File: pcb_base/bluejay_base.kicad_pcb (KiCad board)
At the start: 2 copper layers, 147 x 140.5 mm, 10 parts

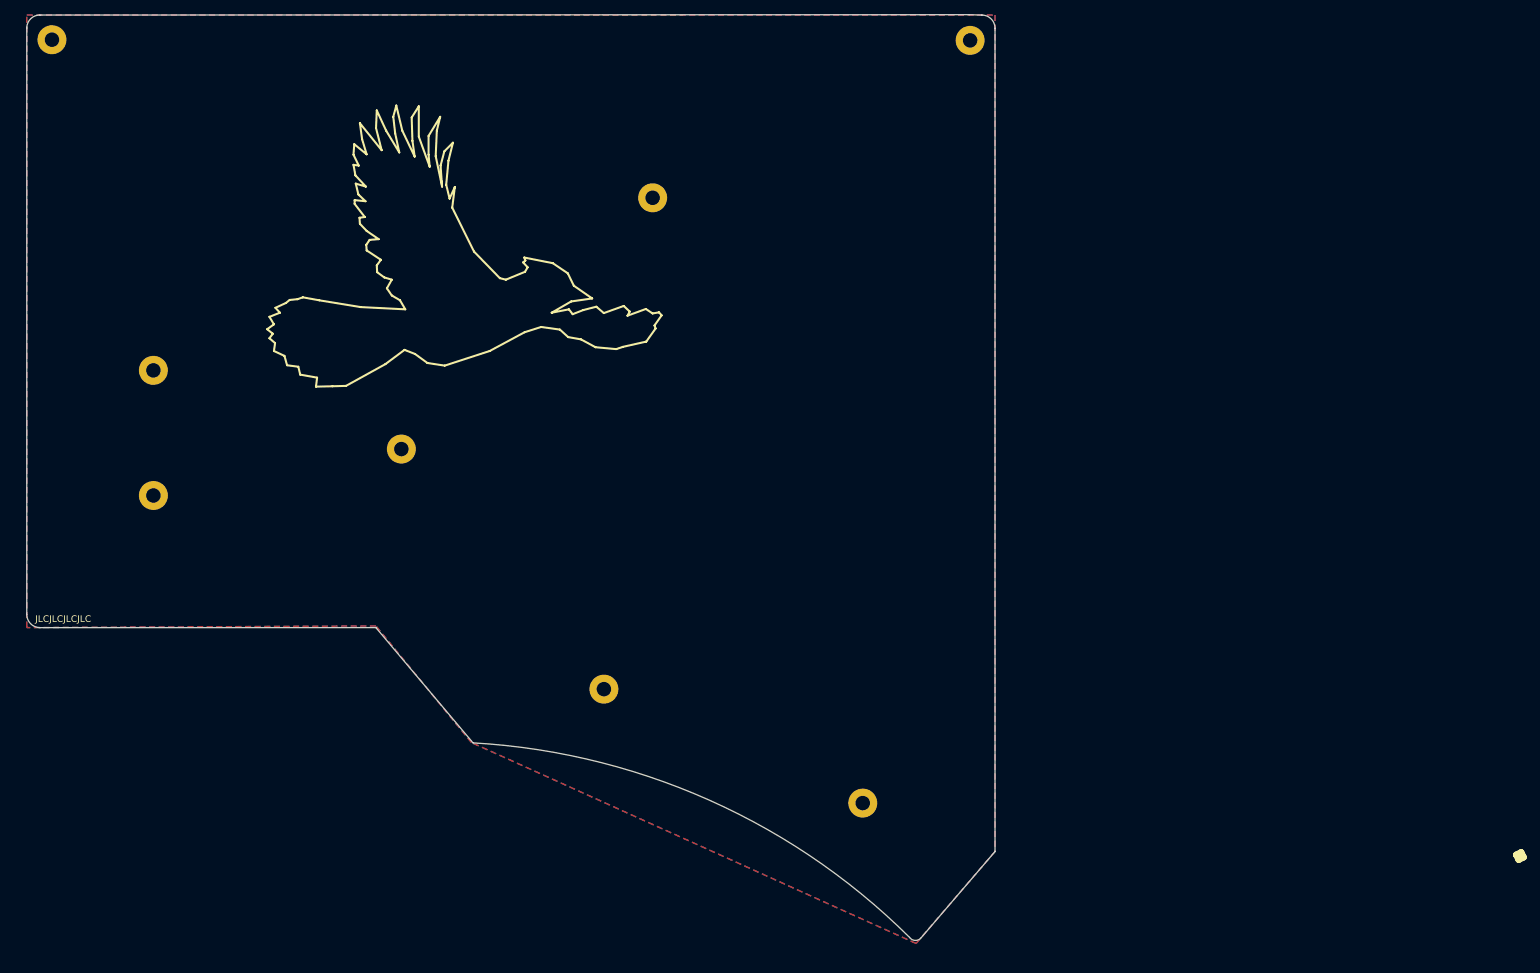
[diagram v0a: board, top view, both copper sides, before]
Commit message: Round edges of PCB
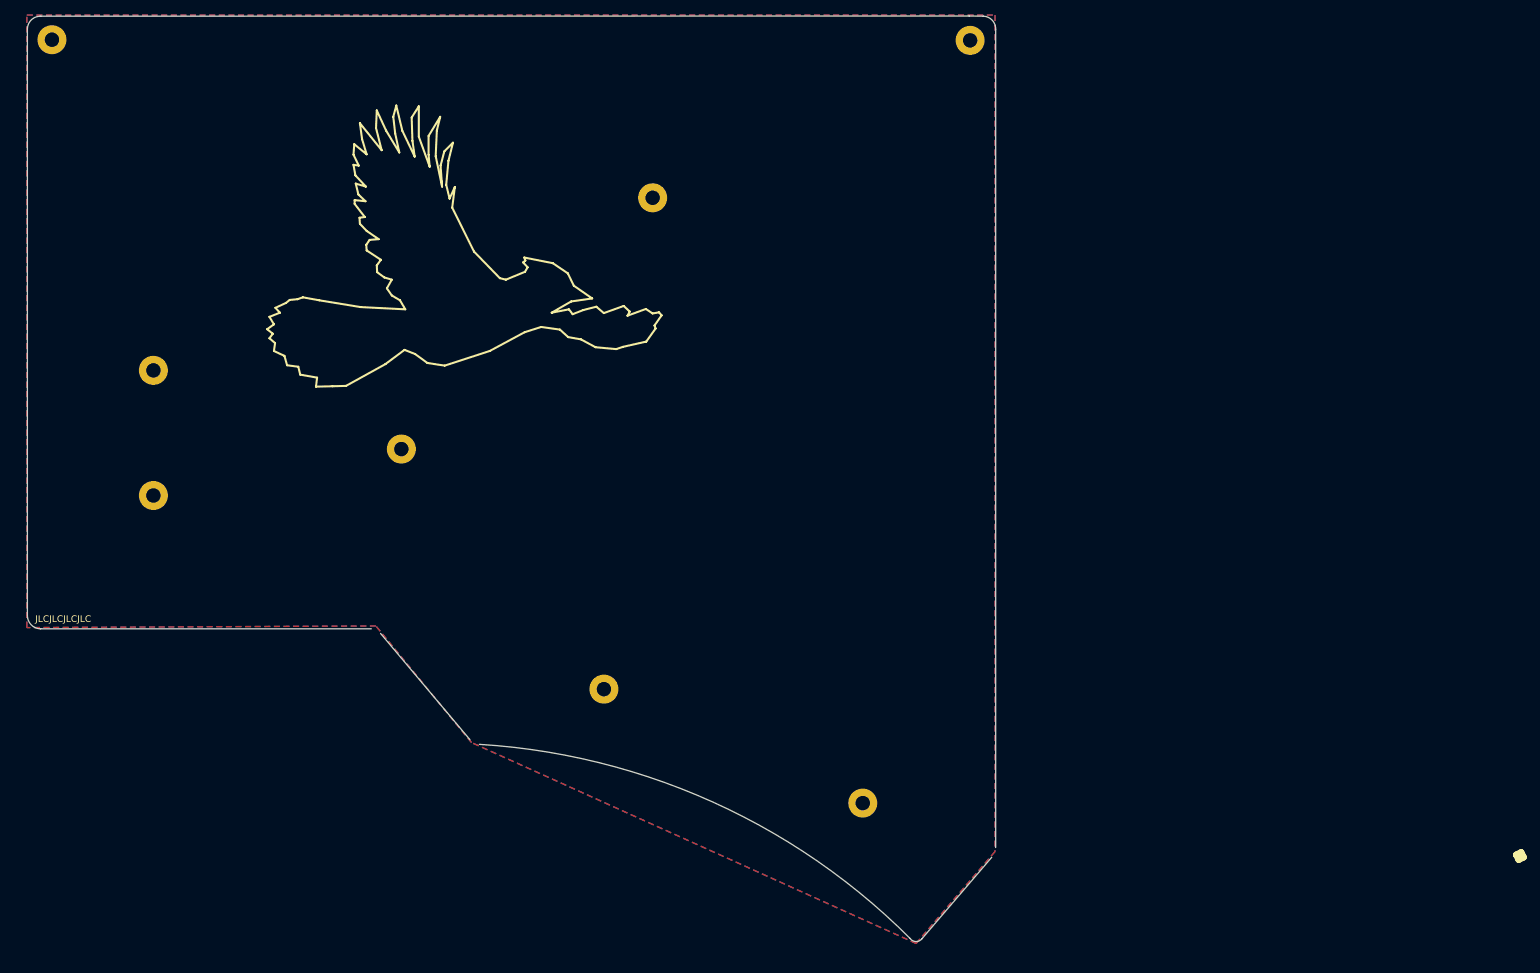
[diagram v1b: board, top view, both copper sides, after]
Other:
- outline, holes or cut-outs redrawn
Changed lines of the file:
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@@
   (gr_line locked (start 26.028999 -42.674998) (end 26.028999 -42.674998) (layer "Eco1.User") (width 0.188976))
   (gr_line locked (start -16.546013 52.286989) (end -16.546013 38.286989) (layer "Eco1.User") (width 0.188976))
-  (gr_line (start 60.9812 70.6563) (end 49.7812 83.7263) (layer "Edge.Cuts") (width 0.1))
-  (gr_arc (start -18.2688 54.1563) (mid 17.583107 62.841492) (end 48.0112 83.6963) (layer "Edge.Cuts") (width 0.1))
-  (gr_arc (start 58.9812 -56.3437) (mid 60.393459 -55.755959) (end 60.981199 -54.3437) (layer "Edge.Cuts") (width 0.1))
-  (gr_line (start 60.9812 70.6563) (end 60.981199 -54.3437) (layer "Edge.Cuts") (width 0.1))
-  (gr_arc (start -86.024489 -54.35145) (mid -85.442713 -55.767431) (end -84.024489 -56.3437) (layer "Edge.Cuts") (width 0.1))
-  (gr_arc (start -84.02552 36.663017) (mid -85.443204 36.061839) (end -86.025519 34.6363) (layer "Edge.Cuts") (width 0.1))
-  (gr_line (start -86.024489 -54.35145) (end -86.025519 34.6363) (layer "Edge.Cuts") (width 0.1))
-  (gr_line (start -84.02552 36.663017) (end -33.0188 36.6563) (layer "Edge.Cuts") (width 0.1))
-  (gr_line (start -33.0188 36.6563) (end -18.2688 54.1563) (layer "Edge.Cuts") (width 0.1))
-  (gr_line (start 58.9812 -56.3437) (end 57.05 -56.4) (layer "Edge.Cuts") (width 0.1))
-  (gr_line (start 57.05 -56.4) (end -84.024489 -56.3437) (layer "Edge.Cuts") (width 0.1))
-  (gr_arc (start 49.7812 83.7263) (mid 48.888799 84.147698) (end 48.0112 83.6963) (layer "Edge.Cuts") (width 0.1))
+  (gr_line (start 60.48 71.53) (end 49.88 83.9) (layer "Edge.Cuts") (width 0.1))
+  (gr_arc (start -17.32 54.38) (mid 18.101214 63.120674) (end 48.11 83.87) (layer "Edge.Cuts") (width 0.1))
+  (gr_arc (start 59.2 -56.175) (mid 60.553201 -55.55994) (end 61.08 -54.17) (layer "Edge.Cuts") (width 0.1))
+  (gr_line (start 61.08 70.05) (end 61.08 -54.17) (layer "Edge.Cuts") (width 0.1))
+  (gr_arc (start -85.93 -54.18) (mid -85.347749 -55.594848) (end -83.93 -56.17) (layer "Edge.Cuts") (width 0.1))
+  (gr_arc (start -83.93 36.84) (mid -85.348353 36.23717) (end -85.93 34.81) (layer "Edge.Cuts") (width 0.1))
+  (gr_line (start -85.93 34.81) (end -85.93 -54.18) (layer "Edge.Cuts") (width 0.1))
+  (gr_line (start -83.93 36.84) (end -33.72 36.84) (layer "Edge.Cuts") (width 0.1))
+  (gr_line (start -32.31 37.54) (end -18.73 53.68) (layer "Edge.Cuts") (width 0.1))
+  (gr_line (start 59.2 -56.175) (end 57.05 -56.2) (layer "Edge.Cuts") (width 0.1))
+  (gr_line (start 57.05 -56.2) (end -83.93 -56.17) (layer "Edge.Cuts") (width 0.1))
+  (gr_arc (start 49.88 83.9) (mid 48.987603 84.321434) (end 48.11 83.87) (layer "Edge.Cuts") (width 0.1))
+  (gr_arc (start -33.72 36.84) (mid -32.960504 37.08023) (end -32.31 37.54) (layer "F.Fab") (width 0.1))
+  (gr_arc (start 61.08 70.05) (mid 60.863331 70.823783) (end 60.48 71.53) (layer "F.Fab") (width 0.1))
+  (gr_arc (start -17.32 54.38) (mid -18.079496 54.13977) (end -18.73 53.68) (layer "F.Fab") (width 0.1))
   (gr_text "JLCJLCJLCJLC" (at -80.5 35.33) (layer "F.SilkS")
     (effects (font (size 1 1) (thickness 0.15)))

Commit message: Update placement of some components and size of drill holes
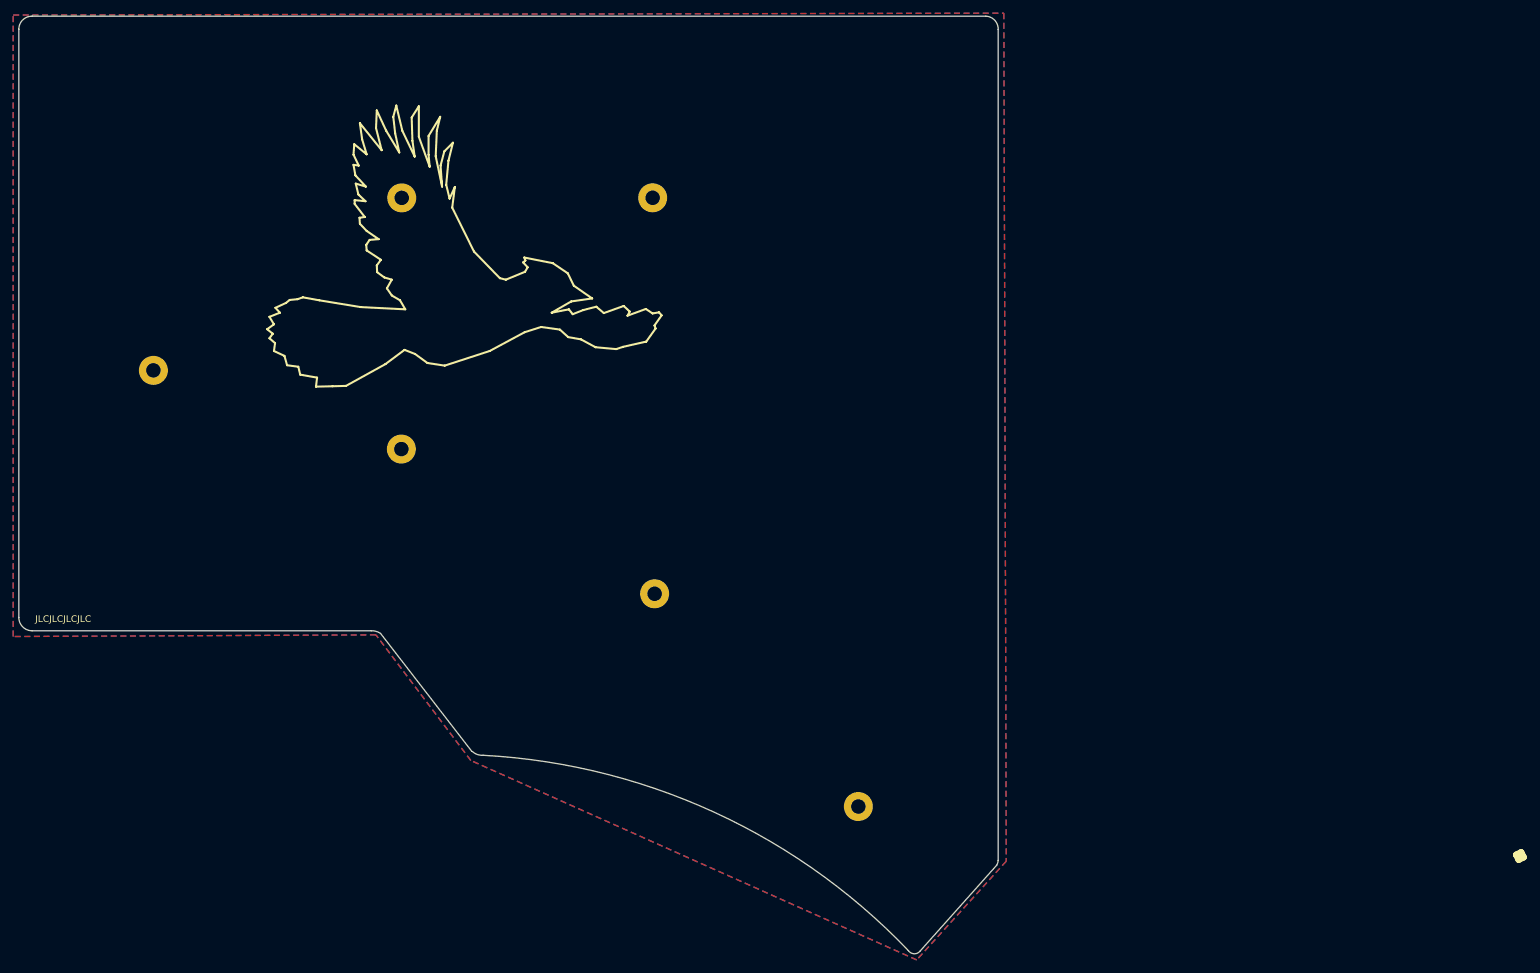
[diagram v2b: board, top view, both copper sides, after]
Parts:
- removed H7, H8: M2, MountingHole:MountingHole_2.2mm_M2_Pad
- moved H2 97.6 mm to (40.2, 63.8)
- moved H6 77.5 mm to (9.30, 31.5)
- moved H1 58.3 mm to (-29.1, -28.6)
- moved H3 53.8 mm to (9.00, -28.6)
- renumbered H3 to H2, H2 to H3
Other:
- board size 147 x 140.5 mm -> 148.7 x 142.3 mm
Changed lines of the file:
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@@
   (net 1 "GND")
-  (footprint "MountingHole:MountingHole_2.2mm_M2_Pad" (layer "F.Cu")
-    (at 40.9 63.3)
-    (descr "Mounting Hole 2.2mm, M2")
-    (tags "mounting hole 2.2mm m2")
-    (property "Sheetfile" "bluejay_base.kicad_sch")
-    (property "Sheetname" "")
-    (property "exclude_from_bom" "")
-    (attr exclude_from_pos_files exclude_from_bom)
-    (fp_text reference "H8" (at 0 -3.2) (layer "F.Fab")
-      (effects (font (size 1 1) (thickness 0.15)))
-    )
-    (fp_text value "M2" (at 0 3.2) (layer "F.Fab")
-      (effects (font (size 1 1) (thickness 0.15)))
-    )
-    (fp_text user "${REFERENCE}" (at 0 0) (layer "F.Fab")
-      (effects (font (size 1 1) (thickness 0.15)))
-    )
-    (fp_circle (center 0 0) (end 2.2 0) (layer "Cmts.User") (width 0.15) (fill none))
-    (fp_circle (center 0 0) (end 2.45 0) (layer "F.CrtYd") (width 0.05) (fill none))
-    (pad "1" thru_hole circle (at 0 0) (size 4.4 4.4) (drill 2.2) (layers *.Cu *.Mask))
-  )
   (footprint "MountingHole:MountingHole_2.2mm_M2_Pad" (layer "F.Cu")
     (at -29.15 9.55)
@@
   )
   (footprint "MountingHole:MountingHole_2.2mm_M2_Pad" (layer "F.Cu")
-    (at -82.2 -52.6)
+    (at -29.09 -28.59)
     (descr "Mounting Hole 2.2mm, M2")
     (tags "mounting hole 2.2mm m2")
@@
     (fp_circle (center 0 0) (end 2.45 0) (layer "F.CrtYd") (width 0.05) (fill none))
     (pad "1" thru_hole circle (at 0 0) (size 4.4 4.4) (drill 2.2) (layers *.Cu *.Mask))
-  )
-  (footprint "MountingHole:MountingHole_2.2mm_M2_Pad" (layer "F.Cu")
-    (at 1.6 46)
-    (descr "Mounting Hole 2.2mm, M2")
-    (tags "mounting hole 2.2mm m2")
-    (property "Sheetfile" "bluejay_base.kicad_sch")
-    (property "Sheetname" "")
-    (property "exclude_from_bom" "")
-    (attr exclude_from_pos_files exclude_from_bom)
-    (fp_text reference "H7" (at 0 -3.2) (layer "F.Fab")
-      (effects (font (size 1 1) (thickness 0.15)))
-    )
-    (fp_text value "M2" (at 0 3.2) (layer "F.Fab")
-      (effects (font (size 1 1) (thickness 0.15)))
-    )
-    (fp_text user "${REFERENCE}" (at 0 0) (layer "F.Fab")
-      (effects (font (size 1 1) (thickness 0.15)))
-    )
-    (fp_circle (center 0 0) (end 2.2 0) (layer "Cmts.User") (width 0.15) (fill none))
-    (fp_circle (center 0 0) (end 2.45 0) (layer "F.CrtYd") (width 0.05) (fill none))
-    (pad "1" thru_hole circle (at 0 0) (size 4.4 4.4) (drill 2.2) (layers *.Cu *.Mask))
-  )
-  (footprint "MountingHole:MountingHole_2.2mm_M2_Pad" (layer "F.Cu")
-    (at 57.2 -52.5)
-    (descr "Mounting Hole 2.2mm, M2")
-    (tags "mounting hole 2.2mm m2")
-    (property "Sheetfile" "bluejay_base.kicad_sch")
-    (property "Sheetname" "")
-    (attr exclude_from_pos_files)
-    (fp_text reference "H2" (at 0 -3.2) (layer "F.Fab")
-      (effects (font (size 1 1) (thickness 0.15)))
-    )
-    (fp_text value "M2" (at 0 3.2) (layer "F.Fab")
-      (effects (font (size 1 1) (thickness 0.15)))
-    )
-    (fp_text user "${REFERENCE}" (at 0 0) (layer "F.Fab")
-      (effects (font (size 1 1) (thickness 0.15)))
-    )
-    (fp_circle (center 0 0) (end 2.2 0) (layer "Cmts.User") (width 0.15) (fill none))
-    (fp_circle (center 0 0) (end 2.45 0) (layer "F.CrtYd") (width 0.05) (fill none))
-    (pad "1" thru_hole circle (at 0 0) (size 4.4 4.4) (drill 2.2) (layers *.Cu *.Mask)
-      (net 1 "GND") (pinfunction "1") (pintype "input"))
   )
   (footprint "MountingHole:MountingHole_2.2mm_M2_Pad" (layer "F.Cu")
@@
     (fp_circle (center 0 0) (end 2.2 0) (layer "Cmts.User") (width 0.15) (fill none))
     (fp_circle (center 0 0) (end 2.45 0) (layer "F.CrtYd") (width 0.05) (fill none))
+    (pad "1" thru_hole circle (at 0 0) (size 4.4 4.4) (drill 2.2) (layers *.Cu *.Mask)
+      (net 1 "GND") (pinfunction "1") (pintype "input"))
+  )
+  (footprint "MountingHole:MountingHole_2.2mm_M2_Pad" (layer "F.Cu")
+    (at 40.23 63.82)
+    (descr "Mounting Hole 2.2mm, M2")
+    (tags "mounting hole 2.2mm m2")
+    (property "Sheetfile" "bluejay_base.kicad_sch")
+    (property "Sheetname" "")
+    (attr exclude_from_pos_files)
+    (fp_text reference "H2" (at 0 -3.2) (layer "F.Fab")
+      (effects (font (size 1 1) (thickness 0.15)))
+    )
+    (fp_text value "M2" (at 0 3.2) (layer "F.Fab")
+      (effects (font (size 1 1) (thickness 0.15)))
+    )
+    (fp_text user "${REFERENCE}" (at 0 0) (layer "F.Fab")
+      (effects (font (size 1 1) (thickness 0.15)))
+    )
+    (fp_circle (center 0 0) (end 2.2 0) (layer "Cmts.User") (width 0.15) (fill none))
+    (fp_circle (center 0 0) (end 2.45 0) (layer "F.CrtYd") (width 0.05) (fill none))
     (pad "1" thru_hole circle (at 0 0) (size 4.4 4.4) (drill 2.2) (layers *.Cu *.Mask))
   )
   (footprint "MountingHole:MountingHole_2.2mm_M2_Pad" (layer "F.Cu")
-    (at -66.8 16.6)
+    (at 9.3 31.52)
     (descr "Mounting Hole 2.2mm, M2")
     (tags "mounting hole 2.2mm m2")
@@
   (gr_line locked (start 26.028999 -42.674998) (end 26.028999 -42.674998) (layer "Eco1.User") (width 0.188976))
   (gr_line locked (start -16.546013 52.286989) (end -16.546013 38.286989) (layer "Eco1.User") (width 0.188976))
-  (gr_line (start 60.48 71.53) (end 49.88 83.9) (layer "Edge.Cuts") (width 0.1))
-  (gr_arc (start -17.32 54.38) (mid 18.101214 63.120674) (end 48.11 83.87) (layer "Edge.Cuts") (width 0.1))
-  (gr_arc (start 59.2 -56.175) (mid 60.553201 -55.55994) (end 61.08 -54.17) (layer "Edge.Cuts") (width 0.1))
-  (gr_line (start 61.08 70.05) (end 61.08 -54.17) (layer "Edge.Cuts") (width 0.1))
-  (gr_arc (start -85.93 -54.18) (mid -85.347749 -55.594848) (end -83.93 -56.17) (layer "Edge.Cuts") (width 0.1))
-  (gr_arc (start -83.93 36.84) (mid -85.348353 36.23717) (end -85.93 34.81) (layer "Edge.Cuts") (width 0.1))
-  (gr_line (start -85.93 34.81) (end -85.93 -54.18) (layer "Edge.Cuts") (width 0.1))
-  (gr_line (start -83.93 36.84) (end -33.72 36.84) (layer "Edge.Cuts") (width 0.1))
-  (gr_line (start -32.31 37.54) (end -18.73 53.68) (layer "Edge.Cuts") (width 0.1))
-  (gr_line (start 59.2 -56.175) (end 57.05 -56.2) (layer "Edge.Cuts") (width 0.1))
-  (gr_line (start 57.05 -56.2) (end -83.93 -56.17) (layer "Edge.Cuts") (width 0.1))
-  (gr_arc (start 49.88 83.9) (mid 48.987603 84.321434) (end 48.11 83.87) (layer "Edge.Cuts") (width 0.1))
+  (gr_line (start 61.23 72.74) (end 49.62 85.75) (layer "Edge.Cuts") (width 0.1))
+  (gr_arc (start -33.72 37.14) (mid -32.98386 37.23023) (end -32.31 37.54) (layer "Edge.Cuts") (width 0.1))
+  (gr_arc (start -16.74 56.04) (mid 18.380681 64.696706) (end 47.83 85.7) (layer "Edge.Cuts") (width 0.1))
+  (gr_arc (start -16.74 56.04) (mid -17.619397 55.917949) (end -18.38 55.46) (layer "Edge.Cuts") (width 0.1))
+  (gr_arc (start 59.58 -56.175) (mid 60.933201 -55.55994) (end 61.46 -54.17) (layer "Edge.Cuts") (width 0.1))
+  (gr_line (start 61.46 72) (end 61.46 -54.17) (layer "Edge.Cuts") (width 0.1))
+  (gr_arc (start -87.23 -54.18) (mid -86.647749 -55.594848) (end -85.23 -56.17) (layer "Edge.Cuts") (width 0.1))
+  (gr_arc (start -85.23 37.14) (mid -86.648353 36.53717) (end -87.23 35.11) (layer "Edge.Cuts") (width 0.1))
+  (gr_line (start -87.23 35.11) (end -87.23 -54.18) (layer "Edge.Cuts") (width 0.1))
+  (gr_line (start -85.23 37.14) (end -33.72 37.14) (layer "Edge.Cuts") (width 0.1))
+  (gr_line (start -32.31 37.54) (end -18.47 55.43) (layer "Edge.Cuts") (width 0.1))
+  (gr_arc (start 61.46 72) (mid 61.386012 72.382747) (end 61.23 72.74) (layer "Edge.Cuts") (width 0.1))
+  (gr_line (start 59.58 -56.17) (end -85.23 -56.17) (layer "Edge.Cuts") (width 0.1))
+  (gr_arc (start 49.59 85.78) (mid 48.690274 86.173968) (end 47.83 85.7) (layer "Edge.Cuts") (width 0.1))
   (gr_arc (start -33.72 36.84) (mid -32.960504 37.08023) (end -32.31 37.54) (layer "F.Fab") (width 0.1))
   (gr_arc (start 61.08 70.05) (mid 60.863331 70.823783) (end 60.48 71.53) (layer "F.Fab") (width 0.1))
@@
     (polygon
       (pts
-        (xy 60.9812 -56.3437)
-        (xy 60.9812 70.6563)
-        (xy 49.000658 84.613239)
-        (xy -18.499342 54.113239)
-        (xy -33.0188 36.4063)
-        (xy -86.0188 36.6563)
-        (xy -86.0188 -56.3437)
+        (xy 62.32 -56.63)
+        (xy 62.686696 72.120286)
+        (xy 49.09 87.11)
+        (xy -18.61 56.83)
+        (xy -33.012659 37.759269)
+        (xy -88.082659 38.009269)
+        (xy -88.0888 -56.3437)
       )
     )
